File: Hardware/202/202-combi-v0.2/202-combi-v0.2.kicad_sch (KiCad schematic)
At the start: 35 parts, among them J1 DM3CS-SF, P3 LEFT-201, P4 RIGHT-201, P8 202-SMART-CAM-P, U1 TXS0104EPWR, U2 TXS0104EPWR, U3 ASE-24.000MHZ-LC-T2, U4 Smart_Cam_Expander_MSP430FR23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, U5 TCA9534PWR, U6 TPS79628DCQ

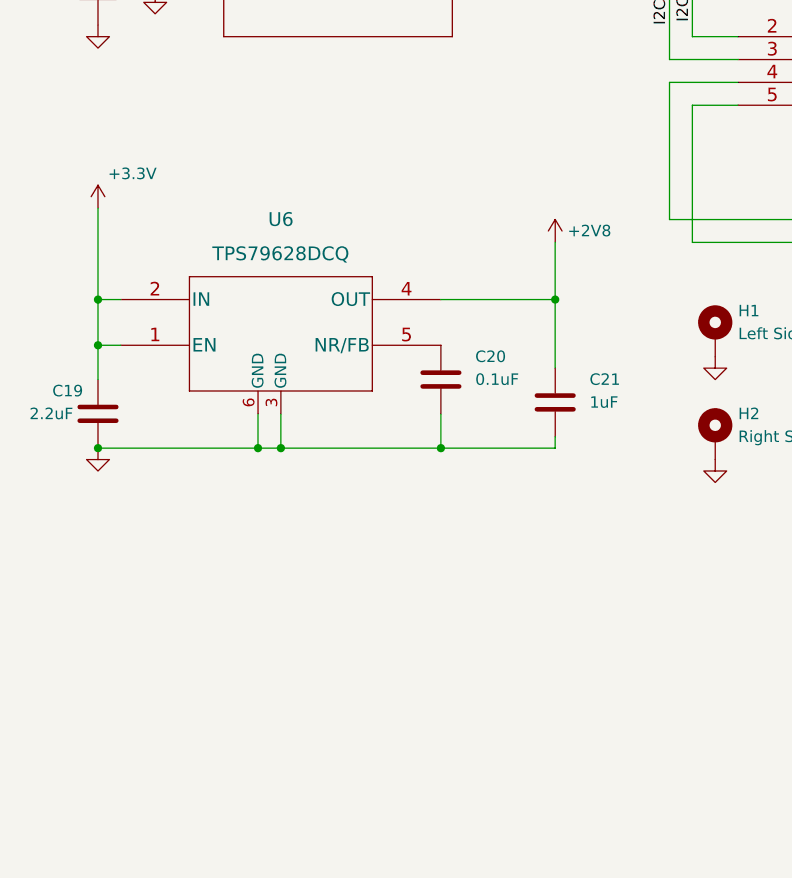
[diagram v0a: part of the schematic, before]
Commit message: Add files via upload
- PCB is converted to 6-layer board
- Differential pairs are routed and matched
- Footprint of the LDO is changed to DFN (TPS79628DRBT is in use now)
- Small changes which were causing DRC errors where corrected in Ziloo footprint library.
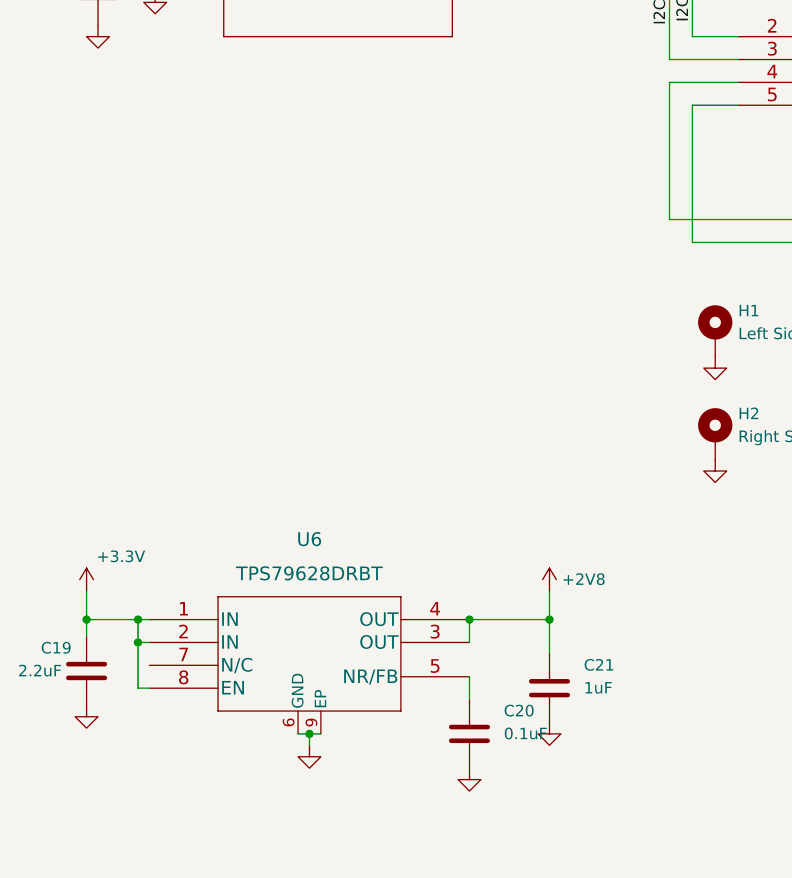
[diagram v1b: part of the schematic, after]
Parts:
- removed U6: TPS79628DCQ, Ziloo:SOT127P706X180-6N, symbol Ziloo:TPS79628DCQ
- added U6: TPS79628DRBT, Ziloo:DFN-8-1EP_3x3mm_P0.65mm_EP1.7x2.05mm, symbol Ziloo:TPS79628DRBT
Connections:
- net +2V8: now also U6.3 (OUT), U6.4 (OUT)
- net +3.3V: now also U6.1 (IN), U6.2 (IN), U6.8 (EN)
- net GND: now also U6.6 (GND), U6.9 (EP)
- net at C20.1: now also U6.5 (NR/FB)
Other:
- moved on the sheet: C19, C20, C21
